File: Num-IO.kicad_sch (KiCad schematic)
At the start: 7 parts, among them U3 74LVC1G18, U4 MAX14851AEE+

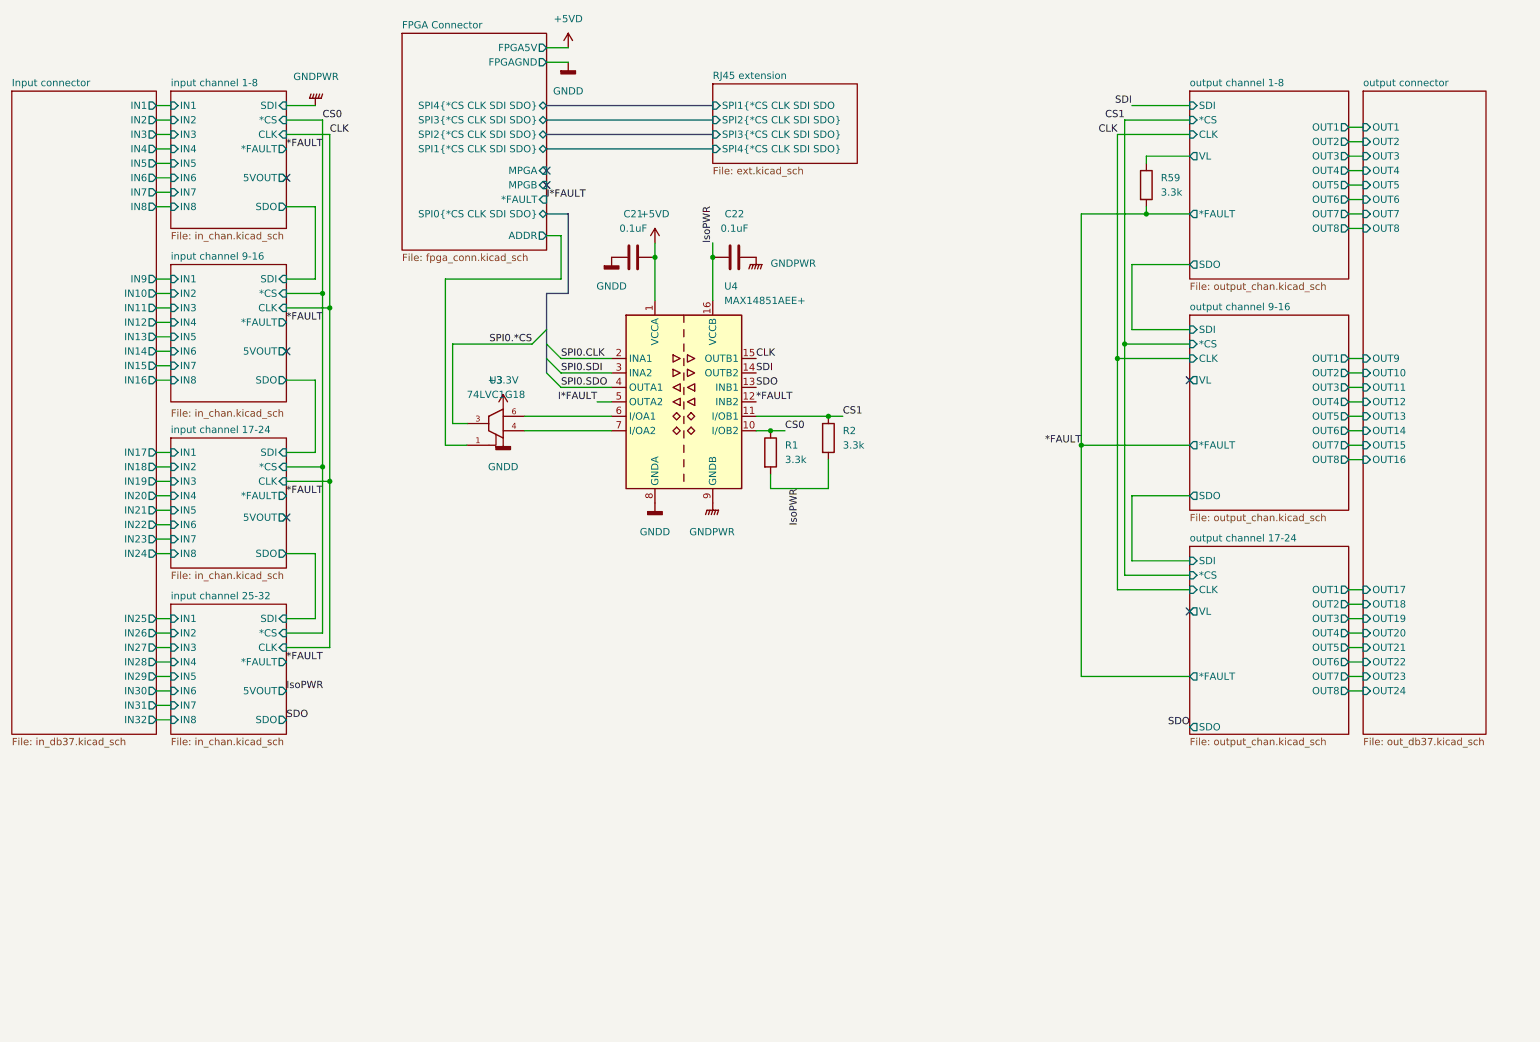
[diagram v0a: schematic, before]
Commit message: Common power stage for field IO
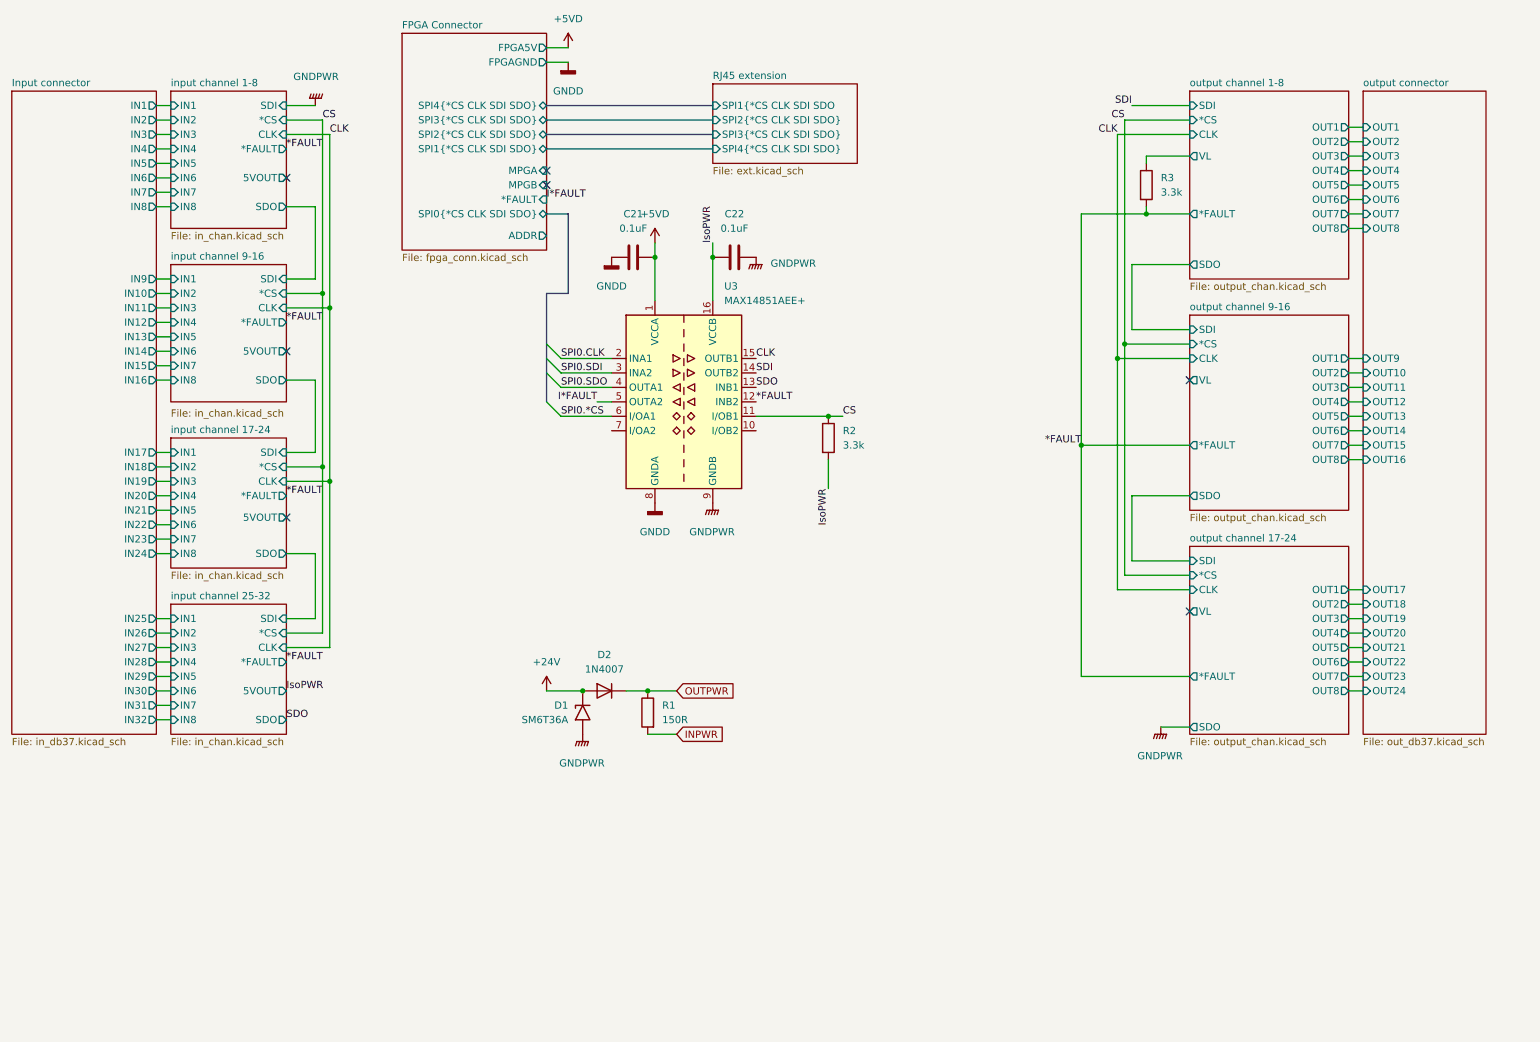
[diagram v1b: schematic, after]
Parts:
- removed U3: 74LVC1G18, Package_TO_SOT_SMD:SOT-23-6, symbol 74xGxx:74LVC1G18
- added D1: SM6T36A, Diode_SMD:D_SMB, symbol Diode:SM6T36A
- added D2: 1N4007, Diode_SMD:D_MELF, symbol Diode:SM4007
- R1: value 3.3k -> 150R; footprint Resistor_SMD:R_0603_1608Metric -> Resistor_SMD:R_0805_2012Metric
- renumbered R59 to R3, U4 to U3
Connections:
- net GNDPWR: now also D1.2 (A2)
- net IsoPWR: no longer R1.2
- net SPI0.*CS: now also U3.6 (I/OA1)
- net CS0: no longer names the net of U3.10 (I/OB2)
- net CS0: no longer R1.1
- net CS1 renamed CS
- net GND renamed GNDD
- new net +24V: D1.1 (A1), D2.2 (A)
- new net INPWR: R1.2
- new net OUTPWR: D2.1 (K), R1.1

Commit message: Further simplifying the schematics
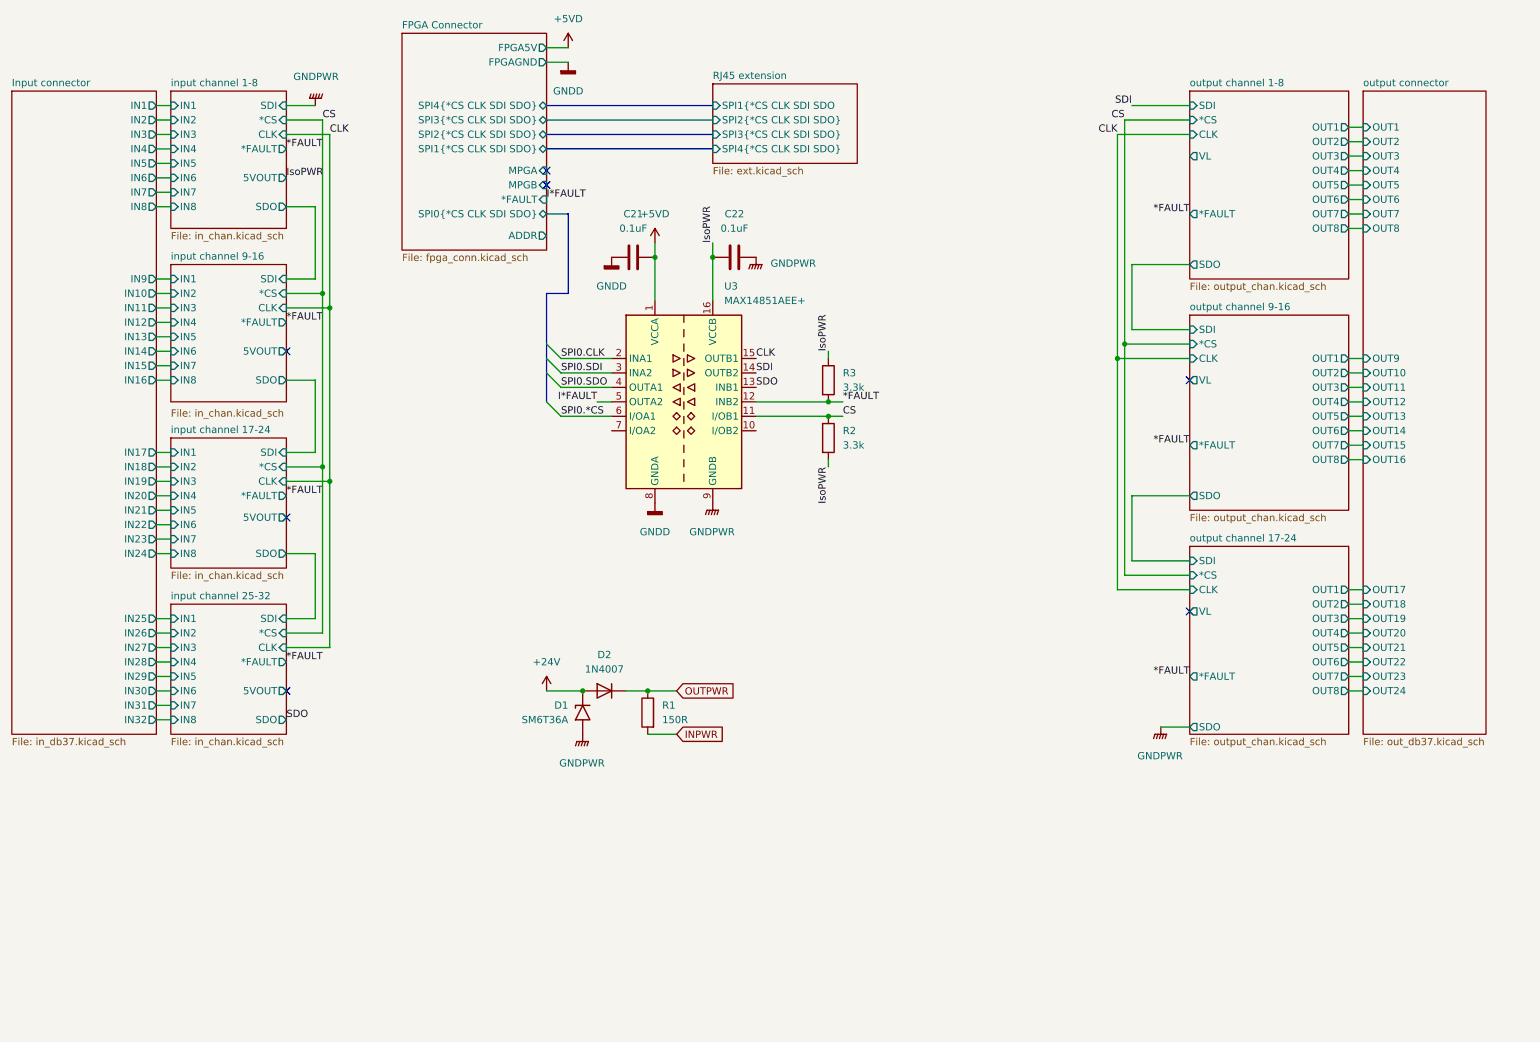
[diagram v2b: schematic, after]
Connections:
- net IsoPWR: now also R3.1
- net output channel 1-8/VL: no longer R3.1
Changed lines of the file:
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@@
   (junction (at 73.66 96.52) (diameter 0) (color 0 0 0 0)
   )
+  (junction (at 161.29 82.55) (diameter 0) (color 0 0 0 0)
+  )
   (junction (at 140.97 57.15) (diameter 0) (color 0 0 0 0)
   )
@@
   (junction (at 161.29 85.09) (diameter 0) (color 0 0 0 0)
   )
-  (junction (at 217.17 49.53) (diameter 0) (color 0 0 0 0)
-  )
   (junction (at 118.11 133.35) (diameter 0) (color 0 0 0 0)
   )
@@
   (junction (at 73.66 66.04) (diameter 0) (color 0 0 0 0)
   )
-  (junction (at 205.74 90.17) (diameter 0) (color 0 0 0 0)
-  )
   (junction (at 212.09 74.93) (diameter 0) (color 0 0 0 0)
   )
-  (no_connect (at 66.04 43.18))
+  (no_connect (at 66.04 133.35))
   (no_connect (at 66.04 73.66))
   (no_connect (at 66.04 102.87))
@@
     (stroke (width 0) (type default) (color 0 0 0 0))
   )
-  (wire (pts (xy 217.17 48.26) (xy 217.17 49.53))
-    (stroke (width 0) (type default) (color 0 0 0 0))
-  )
-  (wire (pts (xy 205.74 90.17) (xy 205.74 130.81))
-    (stroke (width 0) (type default) (color 0 0 0 0))
-  )
   (wire (pts (xy 114.3 74.93) (xy 123.19 74.93))
     (stroke (width 0) (type default) (color 0 0 0 0))
@@
     (stroke (width 0) (type default) (color 0 0 0 0))
   )
+  (wire (pts (xy 163.83 82.55) (xy 161.29 82.55))
+    (stroke (width 0) (type default) (color 0 0 0 0))
+  )
   (wire (pts (xy 66.04 96.52) (xy 73.66 96.52))
     (stroke (width 0) (type default) (color 0 0 0 0))
   )
+  (wire (pts (xy 161.29 82.55) (xy 148.59 82.55))
+    (stroke (width 0) (type default) (color 0 0 0 0))
+  )
   (wire (pts (xy 43.18 120.65) (xy 45.72 120.65))
     (stroke (width 0) (type default) (color 0 0 0 0))
@@
     (stroke (width 0) (type default) (color 0 0 0 0))
   )
-  (wire (pts (xy 224.79 49.53) (xy 217.17 49.53))
-    (stroke (width 0) (type default) (color 0 0 0 0))
-  )
   (wire (pts (xy 129.54 140.97) (xy 134.62 140.97))
     (stroke (width 0) (type default) (color 0 0 0 0))
@@
     (stroke (width 0) (type default) (color 0 0 0 0))
   )
-  (wire (pts (xy 217.17 49.53) (xy 205.74 49.53))
-    (stroke (width 0) (type default) (color 0 0 0 0))
-  )
   (wire (pts (xy 252.73 85.09) (xy 255.27 85.09))
     (stroke (width 0) (type default) (color 0 0 0 0))
@@
     (stroke (width 0) (type default) (color 0 0 0 0))
   )
-  (wire (pts (xy 217.17 39.37) (xy 224.79 39.37))
-    (stroke (width 0) (type default) (color 0 0 0 0))
-  )
   (wire (pts (xy 252.73 44.45) (xy 255.27 44.45))
     (stroke (width 0) (type default) (color 0 0 0 0))
@@
     (stroke (width 0) (type default) (color 0 0 0 0))
   )
-  (wire (pts (xy 161.29 92.71) (xy 161.29 97.79))
+  (wire (pts (xy 161.29 92.71) (xy 161.29 93.98))
     (stroke (width 0) (type default) (color 0 0 0 0))
   )
@@
     (stroke (width 0) (type default) (color 0 0 0 0))
   )
-  (wire (pts (xy 205.74 90.17) (xy 224.79 90.17))
-    (stroke (width 0) (type default) (color 0 0 0 0))
-  )
   (wire (pts (xy 140.97 54.61) (xy 140.97 57.15))
     (stroke (width 0) (type default) (color 0 0 0 0))
@@
     (stroke (width 0) (type default) (color 0 0 0 0))
   )
-  (wire (pts (xy 205.74 130.81) (xy 224.79 130.81))
-    (stroke (width 0) (type default) (color 0 0 0 0))
-  )
   (wire (pts (xy 212.09 74.93) (xy 224.79 74.93))
     (stroke (width 0) (type default) (color 0 0 0 0))
@@
     (stroke (width 0) (type default) (color 0 0 0 0))
   )
-  (wire (pts (xy 205.74 49.53) (xy 205.74 90.17))
-    (stroke (width 0) (type default) (color 0 0 0 0))
-  )
   (bus (pts (xy 111.76 30.48) (xy 140.97 30.48))
     (stroke (width 0) (type default) (color 0 0 0 0))
@@
     (stroke (width 0) (type default) (color 0 0 0 0))
   )
+  (wire (pts (xy 161.29 73.66) (xy 161.29 74.93))
+    (stroke (width 0) (type default) (color 0 0 0 0))
+  )
   (wire (pts (xy 72.39 63.5) (xy 72.39 93.98))
     (stroke (width 0) (type default) (color 0 0 0 0))
@@
   )
   (wire (pts (xy 66.04 66.04) (xy 73.66 66.04))
-    (stroke (width 0) (type default) (color 0 0 0 0))
-  )
-  (wire (pts (xy 217.17 40.64) (xy 217.17 39.37))
     (stroke (width 0) (type default) (color 0 0 0 0))
   )
@@
     (effects (font (size 1.27 1.27)) (justify left bottom))
   )
-  (label "*FAULT" (at 205.74 90.17 180)
+  (label "*FAULT" (at 224.79 49.53 180)
+    (effects (font (size 1.27 1.27)) (justify right bottom))
+  )
+  (label "*FAULT" (at 224.79 130.81 180)
+    (effects (font (size 1.27 1.27)) (justify right bottom))
+  )
+  (label "*FAULT" (at 224.79 90.17 180)
     (effects (font (size 1.27 1.27)) (justify right bottom))
   )
@@
     (effects (font (size 1.27 1.27)) (justify left bottom))
   )
-  (label "*FAULT" (at 148.59 82.55 0)
+  (label "*FAULT" (at 163.83 82.55 0)
     (effects (font (size 1.27 1.27)) (justify left bottom))
   )
@@
     (effects (font (size 1.27 1.27)) (justify right bottom))
   )
-  (label "IsoPWR" (at 161.29 97.79 270)
+  (label "IsoPWR" (at 161.29 93.98 270)
     (effects (font (size 1.27 1.27)) (justify right bottom))
   )
@@
     (effects (font (size 1.27 1.27)) (justify left bottom))
   )
+  (label "IsoPWR" (at 161.29 73.66 90)
+    (effects (font (size 1.27 1.27)) (justify left bottom))
+  )
   (label "CS" (at 213.36 33.02 180)
     (effects (font (size 1.27 1.27)) (justify right bottom))
@@
     (effects (font (size 1.27 1.27)) (justify left bottom))
   )
-  (label "IsoPWR" (at 66.04 133.35 0)
+  (label "IsoPWR" (at 66.04 43.18 0)
     (effects (font (size 1.27 1.27)) (justify left bottom))
   )
@@
     )
     (property "Datasheet" "~" (id 3) (at 127 57.15 0)
-      (effects (font (size 1.27 1.27)) hide)
-    )
-    (pin "1")
-    (pin "2")
-  )
-  (symbol (lib_id "Device:R") (at 217.17 44.45 0) (unit 1)
-    (in_bom yes) (on_board yes) (fields_autoplaced)
-    (property "Reference" "R3" (id 0) (at 219.71 43.1799 0)
-      (effects (font (size 1.27 1.27)) (justify left))
-    )
-    (property "Value" "3.3k" (id 1) (at 219.71 45.7199 0)
-      (effects (font (size 1.27 1.27)) (justify left))
-    )
-    (property "Footprint" "Resistor_SMD:R_0603_1608Metric" (id 2) (at 215.392 44.45 90)
-      (effects (font (size 1.27 1.27)) hide)
-    )
-    (property "Datasheet" "~" (id 3) (at 217.17 44.45 0)
       (effects (font (size 1.27 1.27)) hide)
     )
@@
     (pin "2")
   )
+  (symbol (lib_id "Device:R") (at 161.29 78.74 0) (unit 1)
+    (in_bom yes) (on_board yes) (fields_autoplaced)
+    (property "Reference" "R3" (id 0) (at 163.83 77.4699 0)
+      (effects (font (size 1.27 1.27)) (justify left))
+    )
+    (property "Value" "3.3k" (id 1) (at 163.83 80.0099 0)
+      (effects (font (size 1.27 1.27)) (justify left))
+    )
+    (property "Footprint" "Resistor_SMD:R_0603_1608Metric" (id 2) (at 159.512 78.74 90)
+      (effects (font (size 1.27 1.27)) hide)
+    )
+    (property "Datasheet" "~" (id 3) (at 161.29 78.74 0)
+      (effects (font (size 1.27 1.27)) hide)
+    )
+    (pin "1")
+    (pin "2")
+  )
   (sheet (at 224.79 27.94) (size 27.94 33.02) (fields_autoplaced)
     (stroke (width 0.1524) (type solid) (color 0 0 0 0))
@@
       (reference "R2") (unit 1) (value "3.3k") (footprint "Resistor_SMD:R_0603_1608Metric")
     )
-    (path "/af421f53-30c2-43b8-acf8-c0797fe72217"
+    (path "/ff2fff50-9c09-481e-aa7d-87386764e613"
       (reference "R3") (unit 1) (value "3.3k") (footprint "Resistor_SMD:R_0603_1608Metric")
     )
+    (path "/c9e3a407-39b9-409a-bd2f-25a387b280f7/af3096fe-b8b6-4e0b-8e85-27d183a7fcb8"
+      (reference "R4") (unit 1) (value "4816P-T01-202LF") (footprint "Maxim industrial IO:4816P")
+    )
+    (path "/c9e3a407-39b9-409a-bd2f-25a387b280f7/0d7d938f-7d3a-4351-b1c0-fd19d07f79be"
+      (reference "R5") (unit 1) (value "15k") (footprint "Resistor_SMD:R_0805_2012Metric")
+    )
     (path "/9bb88e24-7dd7-4da3-8728-805be59f14e8/af3096fe-b8b6-4e0b-8e85-27d183a7fcb8"
-      (reference "R4") (unit 1) (value "4816P-T01-202LF") (footprint "Maxim industrial IO:4816P")
+      (reference "R6") (unit 1) (value "4816P-T01-202LF") (footprint "Maxim industrial IO:4816P")
     )
     (path "/9bb88e24-7dd7-4da3-8728-805be59f14e8/0d7d938f-7d3a-4351-b1c0-fd19d07f79be"
-      (reference "R5") (unit 1) (value "15k") (footprint "Resistor_SMD:R_0805_2012Metric")
+      (reference "R7") (unit 1) (value "15k") (footprint "Resistor_SMD:R_0805_2012Metric")
     )
     (path "/b82bf96f-9ca1-4070-a6ff-f9982f9e29e2/af3096fe-b8b6-4e0b-8e85-27d183a7fcb8"
-      (reference "R6") (unit 1) (value "4816P-T01-202LF") (footprint "Maxim industrial IO:4816P")
+      (reference "R8") (unit 1) (value "4816P-T01-202LF") (footprint "Maxim industrial IO:4816P")
     )
     (path "/b82bf96f-9ca1-4070-a6ff-f9982f9e29e2/0d7d938f-7d3a-4351-b1c0-fd19d07f79be"
-      (reference "R7") (unit 1) (value "15k") (footprint "Resistor_SMD:R_0805_2012Metric")
-    )
-    (path "/c9e3a407-39b9-409a-bd2f-25a387b280f7/af3096fe-b8b6-4e0b-8e85-27d183a7fcb8"
-      (reference "R8") (unit 1) (value "4816P-T01-202LF") (footprint "Maxim industrial IO:4816P")
-    )
-    (path "/c9e3a407-39b9-409a-bd2f-25a387b280f7/0d7d938f-7d3a-4351-b1c0-fd19d07f79be"
       (reference "R9") (unit 1) (value "15k") (footprint "Resistor_SMD:R_0805_2012Metric")
     )

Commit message: fix DRC errors
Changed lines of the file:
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@@
     (effects (font (size 1.27 1.27)) (justify left bottom))
   )
-  (global_label "INPWR" (shape input) (at 134.62 140.97 0) (fields_autoplaced)
+  (global_label "INPWR" (shape output) (at 134.62 140.97 0) (fields_autoplaced)
     (effects (font (size 1.27 1.27)) (justify left))
     (property "Intersheet References" "${INTERSHEET_REFS}" (id 0) (at 142.9598 140.8906 0)
@@
     )
   )
-  (global_label "OUTPWR" (shape input) (at 134.62 133.35 0) (fields_autoplaced)
+  (global_label "OUTPWR" (shape output) (at 134.62 133.35 0) (fields_autoplaced)
     (effects (font (size 1.27 1.27)) (justify left))
     (property "Intersheet References" "${INTERSHEET_REFS}" (id 0) (at 144.6531 133.2706 0)
